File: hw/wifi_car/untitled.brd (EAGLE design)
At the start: 35.5 x 52.4 mm, 54 parts, among them IC1 LPC1114FBD48, U1 MCP16301T-I/CHY

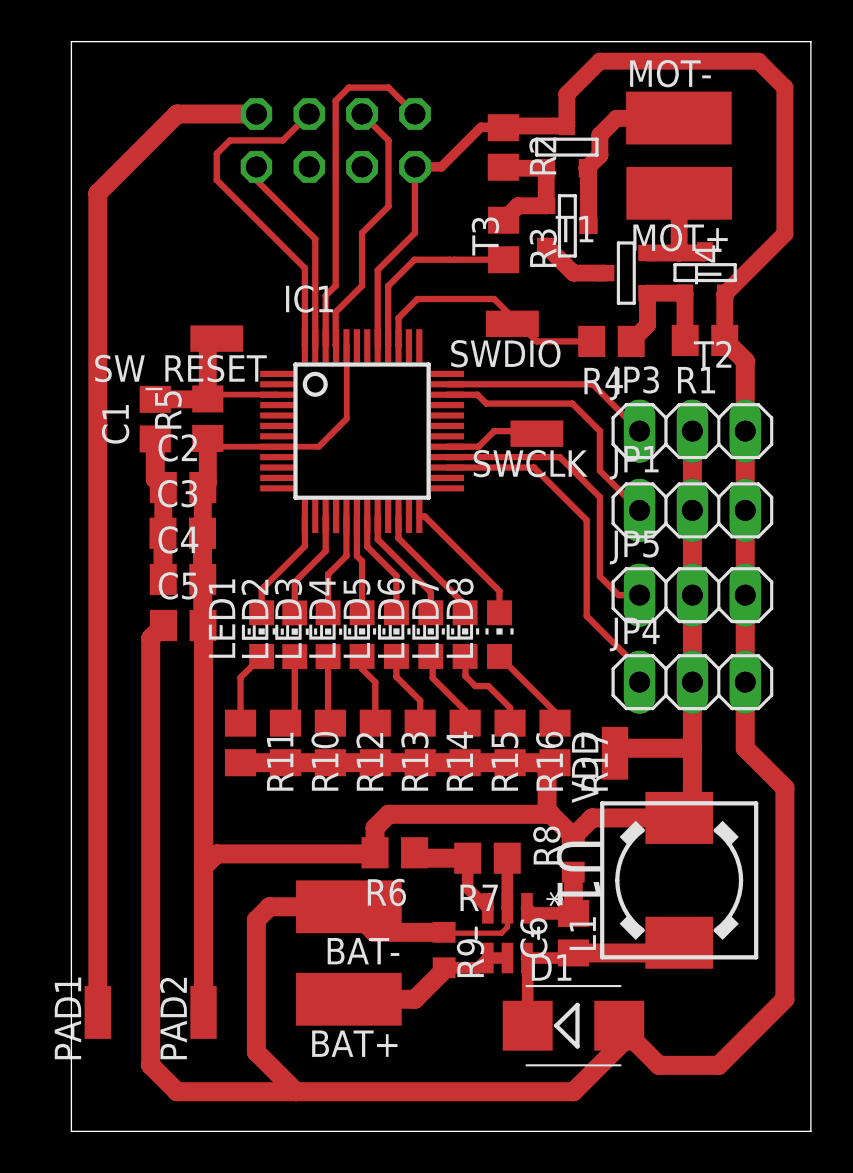
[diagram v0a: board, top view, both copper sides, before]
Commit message: Added ADC for battery measurements
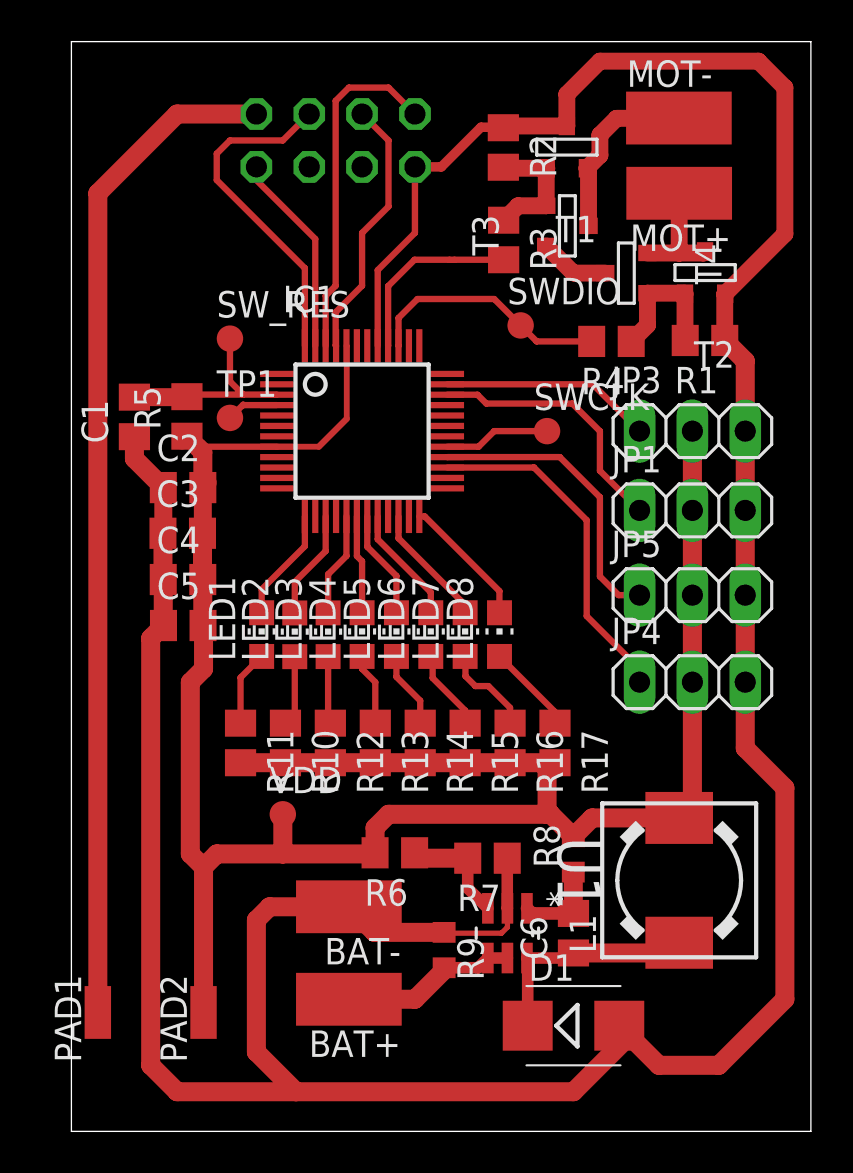
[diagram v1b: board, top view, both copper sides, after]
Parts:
- removed SW_RESET: (no value), wirepad:SMD1,27-2,54
- added SW_RES, TP1: TPB1,27, testpad:B1,27
- SWCLK, SWDIO, VDD: value (none) -> TPB1,27; device wirepad:SMD1,27-2,54 -> testpad:B1,27
- moved VDD 16.2 mm to (14.0, -3.81)
- moved R5 1.01 mm to (9.36, 15.3)
- moved C1 1.01 mm to (6.84, 15.3)
- moved SWCLK 0.50 mm to (26.7, 14.6), turned to 0 degrees
- moved SWDIO 0.40 mm to (25.4, 19.7), turned to 0 degrees
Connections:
- removed net LED10: IC1.22, LED7.C
- removed net LED12: IC1.24, LED8.C
- new net N$18: IC1.4, TP1.TP
- net LED2: now also IC1.15, LED2.C; no longer IC1.14
- net LED3: now also IC1.17, LED3.C; no longer IC1.15, LED2.C
- net LED4: now also IC1.18, LED4.C; no longer IC1.16
- net LED5: now also IC1.19, LED5.C; no longer IC1.17, LED3.C
- net LED6: now also IC1.20, LED6.C; no longer IC1.18, LED4.C
- net LED7: now also IC1.22, LED7.C; no longer IC1.19, LED5.C
- net LED8: now also IC1.24, LED8.C; no longer IC1.20, LED6.C
- net PWM12: now also SWCLK.TP; no longer SWCLK.1
- net PWM2: now also SWDIO.TP; no longer SWDIO.1
- net SW_RESET: now also SW_RES.TP; no longer SW_RESET.1
- net VDD: now also VDD.TP; no longer VDD.1
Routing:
- net LED12: track 6.38 -> 0.00 mm
- net LED10: track 5.96 -> 0.00 mm
- net LED2: track 0.00 -> 5.25 mm
- net LED4: track 0.00 -> 4.73 mm
- net GND: track 165.3 -> 168.0 mm
- net N$18: track 0.00 -> 2.52 mm
- net LED6: track 4.73 -> 5.69 mm
- net SW_RESET: track 9.01 -> 9.94 mm
- net LED7: track 5.21 -> 5.96 mm
- net LED8: track 5.69 -> 6.38 mm

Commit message: Board and schematic update
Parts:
- removed PAD1, PAD2: (no value), wirepad:SMD1,27-2,54
- added C7, C8, C9: 10u, rcl:C0805
- added R18: 11k, rcl:R0805
- R9: value (none) -> 34k; device rcl:R0603 -> rcl:R0805
- moved R9 17.0 mm to (26.7, 5.90)
- moved SWDIO 1.42 mm to (24.1, 19.1)
- moved BAT+ 0.63 mm to (17.1, -12.1)
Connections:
- removed net LED11: IC1.23
- removed net LED9: IC1.21
- removed net N$7: JP2.8, PAD1.1
- removed net N$9: BAT+.1, R9.2, U1.4, U1.5
- new net ADC: IC1.30, R18.2, R9.1
- net BAT+: now also BAT+.1, C7.2, R9.2, U1.4, U1.5
- net GND: now also C7.1, C8.1, C9.1, R18.1; no longer R9.1
- net VDD: now also C8.2, C9.2, JP2.8; no longer PAD2.1
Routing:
- net BAT+: track 3.37 -> 70.4 mm, vias 0 -> 3
- net N$7: track 48.6 -> 0.00 mm
- net VDD: track 105.4 -> 152.5 mm, vias 0 -> 1
- net GND: track 168.0 -> 192.1 mm, vias 0 -> 1
- net ADC: track 0.00 -> 13.5 mm
- net N$9: track 8.51 -> 0.00 mm
